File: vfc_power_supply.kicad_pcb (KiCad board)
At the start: 4 copper layers, 160 x 160 mm, 147 parts, among them J1 Conn_01x03_Male, J2 Conn_01x06_Female, J3 Conn_01x02_Male, J4 Raspberry_Pi_4B, J5 Connector_RJ45_Magjack_Abraco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, J6 Connector_RJ45_Magjack_Abraco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, J7 Conn_01x06_Female, J8 Conn_01x06_Female, J9 Conn_01x06_Female, M1 Logo_10mmx10mm, U1 LT8653S, U10 PCT2075D, U11 ADS7924, U12 VO615A, U13 VO615A, U14 VO615A, U15 VO615A, U16 VO615A, U17 VO615A, U2 LT8636, U3 FPF2701MPX, U4 FPF2701MPX, U5 LM3480-3.3, U6 LM4040DBZ-3, U7 ADS7924, U8 ISO1540, U9 LM4040DBZ-3

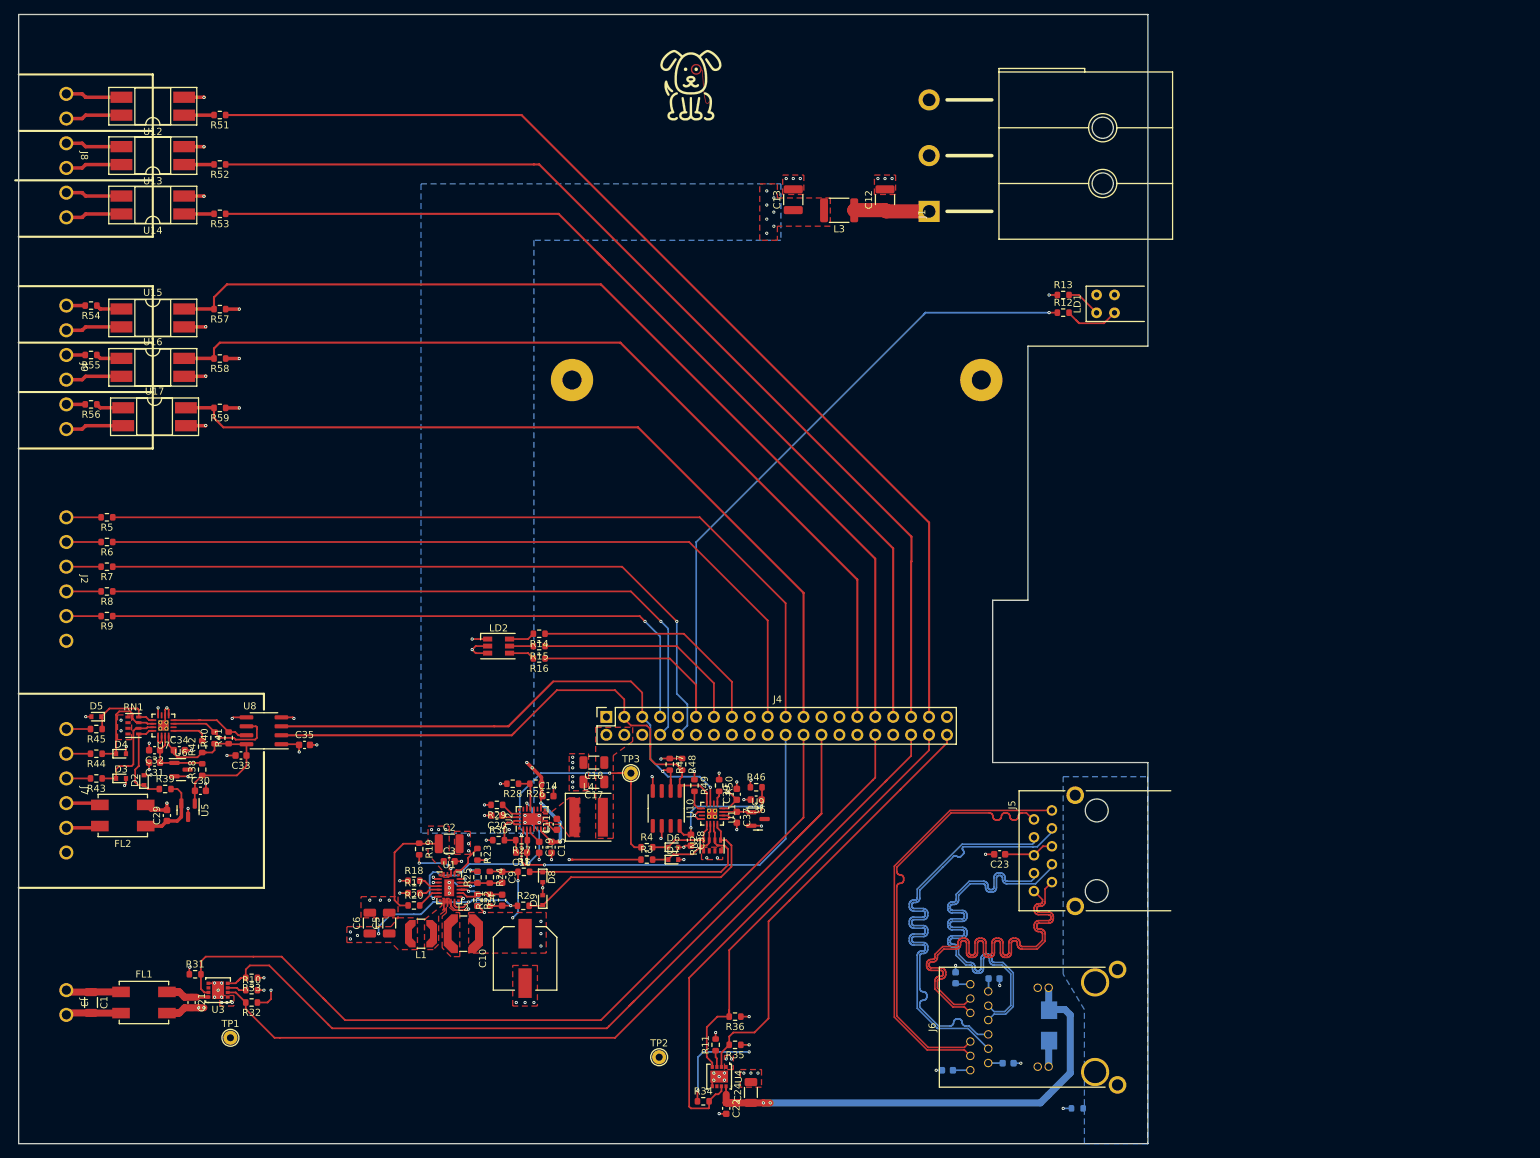
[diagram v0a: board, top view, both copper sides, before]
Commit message: Finished tidying up silkscreen
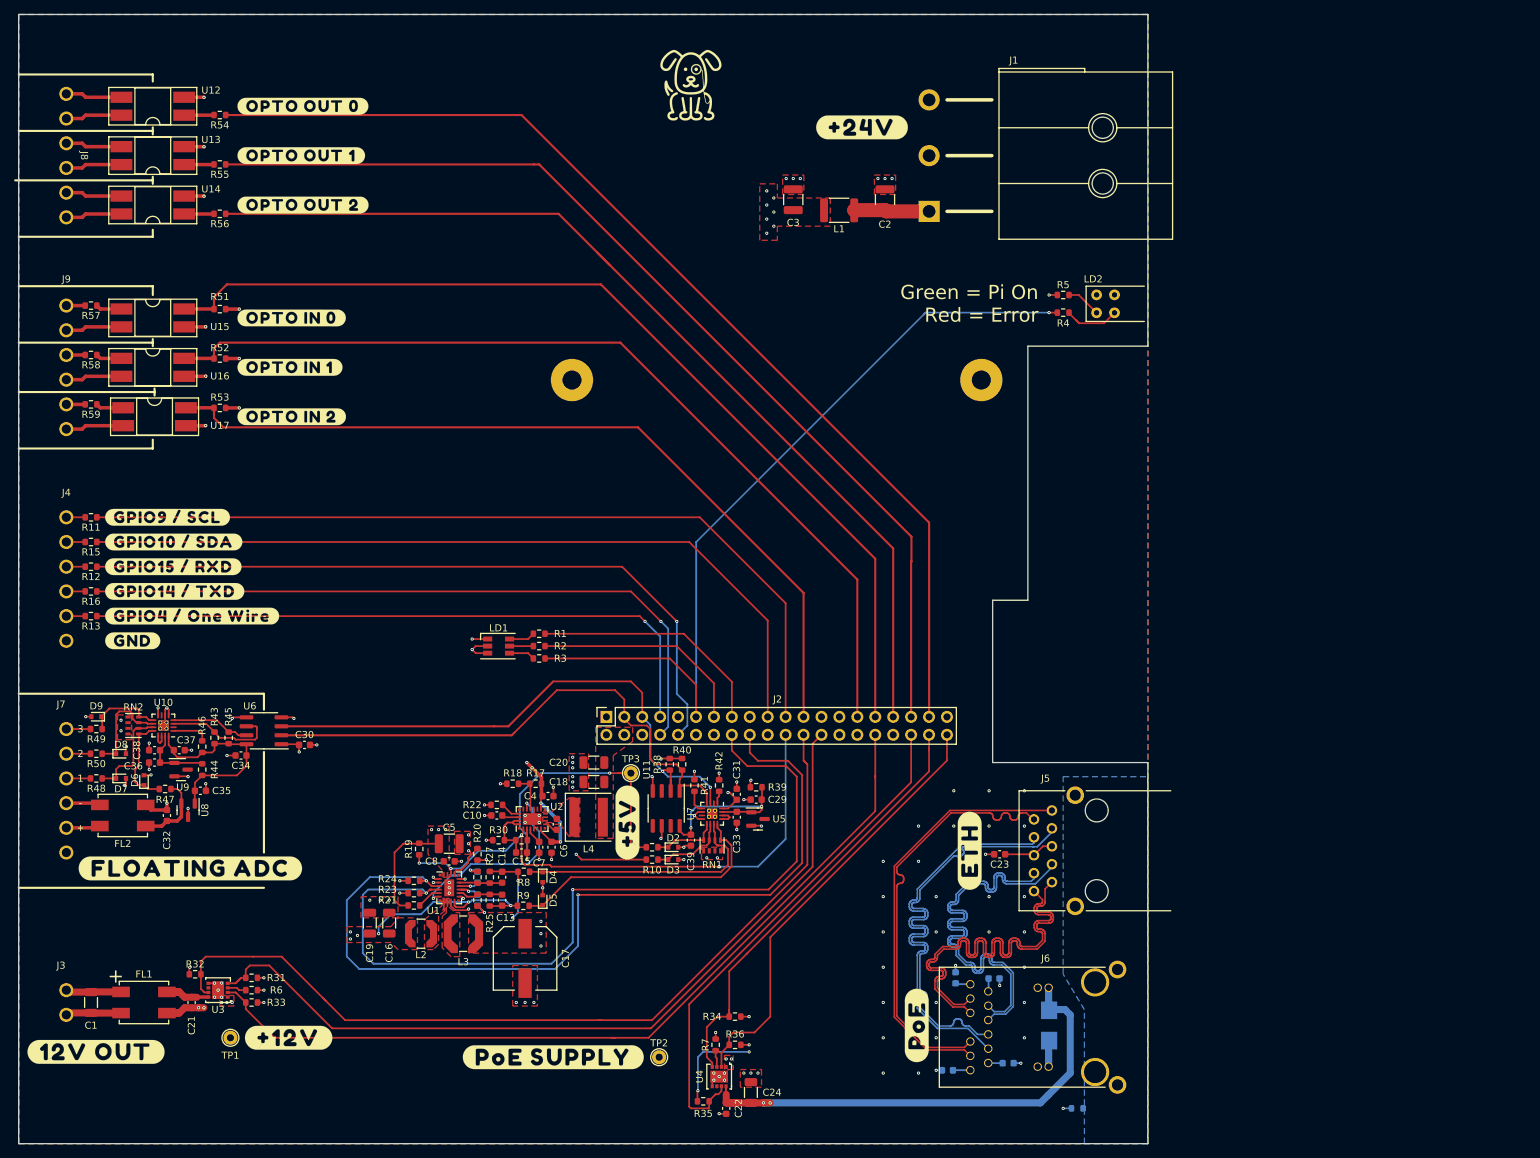
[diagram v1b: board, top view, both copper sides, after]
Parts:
- added ?: , buzzardLabel, F.Cu at (32.2, 103.8)
- added ?: , buzzardLabel, F.Cu at (95.8, 162.8)
- added ?: , buzzardLabel, F.Cu at (51.0, 65.0)
- added ?: , buzzardLabel, F.Cu at (32.2, 86.2)
- added ?: , buzzardLabel, F.Cu at (154.8, 133.5)
- added ?: , buzzardLabel, F.Cu at (32.2, 89.8)
- added ?: , buzzardLabel, F.Cu at (51.0, 35.0)
- added ?: , buzzardLabel, F.Cu at (133.0, 31.0)
- added ?: , buzzardLabel, F.Cu at (32.2, 93.2)
- added ?: , buzzardLabel, F.Cu at (28.5, 136.0)
- added ?: , buzzardLabel, F.Cu at (106.2, 129.5)
- added ?: , buzzardLabel, F.Cu at (51.0, 72.0)
- added ?: , buzzardLabel, F.Cu at (32.2, 96.8)
- added ?: , buzzardLabel, F.Cu at (58.2, 160.0)
- added ?: , buzzardLabel, F.Cu at (21.2, 162.0)
- added ?: , buzzardLabel, F.Cu at (51.0, 28.0)
- added ?: , buzzardLabel, F.Cu at (51.0, 42.0)
- added ?: , buzzardLabel, F.Cu at (51.0, 58.0)
- added ?: , buzzardLabel, F.Cu at (147.2, 158.2)
- added ?: , buzzardLabel, F.Cu at (32.2, 100.2)
- moved R11 2.25 mm to (30.2, 86.2)
- moved R12 2.25 mm to (30.2, 93.2)
- moved R13 2.25 mm to (30.2, 100.2)
- moved R15 2.25 mm to (30.2, 89.8)
- moved R16 2.25 mm to (30.2, 96.8)
- moved R10 0.75 mm to (109.8, 134.8)
- moved R14 0.75 mm to (109.8, 133.0)
- renumbered C20 to C10, C8 to C11, C11 to C12, C4 to C13, C9 to C14, C16 to C15, C5 to C16, C10 to C17, C17 to C18, C6 to C19, C12 to C2, C18 to C20, C36 to C29, C13 to C3, C35 to C30, C39 to C31, C29 to C32, C37 to C33, C33 to C34, C30 to C35, C31 to C36, C34 to C37, C32 to C38, C38 to C39, C14 to C4, C2 to C5, C15 to C6, C19 to C7, C3 to C8, C7 to C9, D6 to D2, D7 to D3, D8 to D4, D9 to D5, D2 to D6, D3 to D7, D4 to D8, D5 to D9, J4 to J2, J2 to J4, L3 to L1, L1 to L2, L2 to L3, LD2 to LD1, LD1 to LD2, R14 to R1, R3 to R10, R5 to R11, R7 to R12, R9 to R13, R4 to R14, R6 to R15, R8 to R16, R26 to R17, R28 to R18, R15 to R2, R23 to R20, R20 to R21, R29 to R22, R17 to R23, R18 to R24, R21 to R25, R22 to R26, R24 to R27, R25 to R28, R27 to R29, R16 to R3, R33 to R31, R31 to R32, R32 to R33, R36 to R34, R34 to R35, R35 to R36, R47 to R38, R46 to R39, R12 to R4, R48 to R40, R49 to R41, R50 to R42, R40 to R43, R38 to R44, R41 to R45, R42 to R46, R39 to R47, R43 to R48, R45 to R49, R13 to R5, R44 to R50, R57 to R51, R58 to R52, R59 to R53, R51 to R54, R52 to R55, R53 to R56, R54 to R57, R55 to R58, R56 to R59, R10 to R6, R11 to R7, R1 to R8, R2 to R9, RN2 to RN1, RN1 to RN2, U7 to U10, U10 to U11, U9 to U5, U8 to U6, U11 to U7, U5 to U8, U6 to U9
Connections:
- net /PoE Injector/VDD_AP renamed /PoE Load Switch/VOUT
- net no_connect_(J1-Pad2) renamed no_connect_123
- net no_connect_(J4-Pad1) renamed no_connect_124
- net no_connect_(J4-Pad12) renamed no_connect_125
- net no_connect_(J4-Pad27) renamed no_connect_126
- net no_connect_(J4-Pad28) renamed no_connect_127
- net no_connect_(J6-Pad13) renamed no_connect_128
- net no_connect_(J6-Pad14) renamed no_connect_129
- net no_connect_(J7-Pad6) renamed no_connect_130
- net no_connect_(U10-Pad3) renamed no_connect_133
- net no_connect_(U10-Pad5) renamed no_connect_134
- net no_connect_(U10-Pad7) renamed no_connect_135
- net no_connect_(U11-Pad2) renamed no_connect_137
- net no_connect_(U11-Pad7) renamed no_connect_138
- net no_connect_(U2-Pad16) renamed no_connect_136
- net no_connect_(U7-Pad2) renamed no_connect_131
- net no_connect_(U7-Pad7) renamed no_connect_132
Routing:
- net /PGOOD_21V: track 3.09 -> 124.0 mm, vias 0 -> 2
- net /PGOOD_12V: track 2.98 -> 118.5 mm, vias 0 -> 2
- net /PGOOD_5V: track 65.4 -> 77.6 mm
- net /VIN_CLEAN: track 54.7 -> 44.2 mm, vias 16 -> 15
- net /~FAULT_SWITCH: track 118.8 -> 124.1 mm
- net /PGOOD_SWITCH: track 116.3 -> 119.8 mm
- net /~EN_SWITCH: track 120.8 -> 117.7 mm
- net /GPIO15/RXD: track 100.4 -> 103.0 mm
- net +3V3: track 44.9 -> 42.5 mm
- net Net-(C11-Pad1): track 5.25 -> 2.81 mm
- net /GPIO14/TXD: track 96.4 -> 98.8 mm
- net /GPIO10/SDA: track 111.1 -> 113.4 mm
- net Net-(J4-Pad5): track 4.93 -> 2.68 mm
- net Net-(J4-Pad4): track 4.93 -> 2.68 mm
- net Net-(J4-Pad3): track 4.93 -> 2.68 mm
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- added copper zone on In2.Cu, net /VIN_CLEAN
- added copper zone on B.Cu, net GND
- added copper zone on In2.Cu, net GND
- removed copper zone on B.Cu, net /VIN_CLEAN
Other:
- board text added: "+"
- board text added: "-"
- board text added: "1"
- board text added: "2"
- board text added: "3"
- board text added: "Green = Pi On Red = Error"

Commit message: Ready for review
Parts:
- moved ? 50.0 mm to (82.2, 103.8)
- moved ? 50.0 mm to (145.8, 162.8)
- moved ? 50.0 mm to (101.0, 65.0)
- moved ? 50.0 mm to (82.2, 86.2)
- moved ? 50.0 mm to (204.8, 133.5)
- moved ? 50.0 mm to (82.2, 89.8)
- moved ? 50.0 mm to (101.0, 35.0)
- moved ? 50.0 mm to (183.0, 31.0)
- moved ? 50.0 mm to (82.2, 93.2)
- moved ? 50.0 mm to (78.5, 136.0)
- moved ? 50.0 mm to (156.2, 129.5)
- moved ? 50.0 mm to (101.0, 72.0)
- moved ? 50.0 mm to (82.2, 96.8)
- moved ? 50.0 mm to (108.2, 160.0)
- moved ? 50.0 mm to (71.2, 162.0)
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
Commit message: Added changes following review from RMC
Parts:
- added R60: 100, Resistor_SMD:R_0603_1608Metric, F.Cu at (103.0, 149.8)
- added R61: 100, Resistor_SMD:R_0603_1608Metric, F.Cu at (171.5, 155.2)
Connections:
- net /PoE Load Switch/VOUT renamed /PoE Injector/VDD_AP
- net no_connect_123 renamed no_connect_(J1-Pad2)
- net no_connect_125 renamed no_connect_(J2-Pad12)
- net no_connect_126 renamed no_connect_(J2-Pad27)
- net no_connect_127 renamed no_connect_(J2-Pad28)
- net no_connect_128 renamed no_connect_(J6-Pad13)
- net no_connect_129 renamed no_connect_(J6-Pad14)
- net no_connect_130 renamed no_connect_(J7-Pad6)
- net no_connect_131 renamed no_connect_(U10-Pad2)
- net no_connect_132 renamed no_connect_(U10-Pad7)
- net no_connect_133 renamed no_connect_(U11-Pad3)
- net no_connect_134 renamed no_connect_(U11-Pad5)
- net no_connect_135 renamed no_connect_(U11-Pad7)
- net no_connect_136 renamed no_connect_(U2-Pad16)
- net no_connect_137 renamed no_connect_(U7-Pad2)
- net no_connect_138 renamed no_connect_(U7-Pad7)
- J2 pad 1: no_connect_124 -> +3V3
- R31 pad 2: /~EN_SWITCH -> /Network Switch Load Switch/~EN
- R34 pad 2: /~EN_POE -> /PoE Load Switch/~EN
- U3 pad 4: /~EN_SWITCH -> /Network Switch Load Switch/~EN
- U4 pad 4: /~EN_POE -> /PoE Load Switch/~EN
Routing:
- net /~EN_POE: track 62.8 -> 49.7 mm
- net /PoE Load Switch/~EN: track 0.00 -> 11.7 mm
- net /~EN_SWITCH: track 117.7 -> 111.1 mm
- net /Network Switch Load Switch/~EN: track 0.00 -> 5.58 mm
